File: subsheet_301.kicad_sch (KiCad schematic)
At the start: 12 parts, among them J1601 Like MegaSTE J402, J301 DB-19S ACSI Port, U302 74LS245_PHY, U306 74LS74_PHY, U307 74LS244_PHY

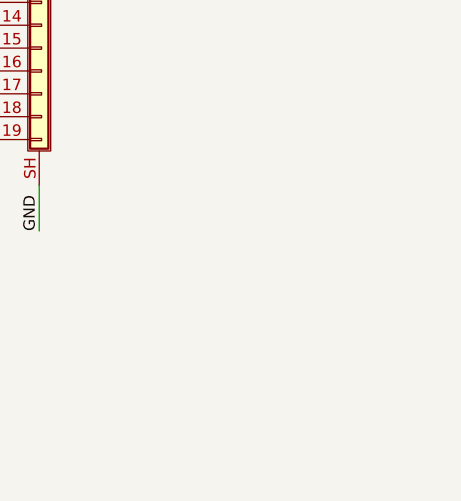
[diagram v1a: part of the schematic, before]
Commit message: add gnd/vcc symbol to start replacing local labels
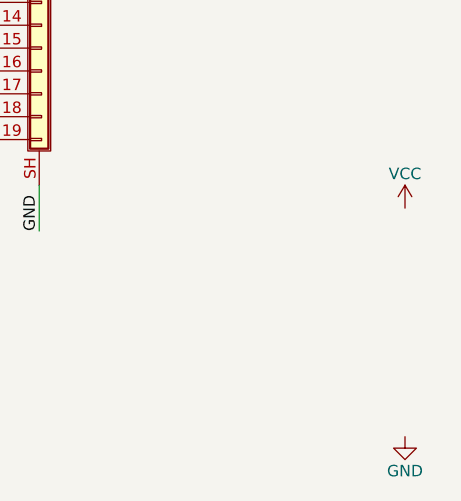
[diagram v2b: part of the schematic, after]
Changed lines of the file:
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@@
     (pin "2")
   )
+  (symbol (lib_id "power:GND") (at 184.15 241.3 0) (unit 1)
+    (in_bom yes) (on_board yes)
+    (property "Reference" "#PWR?" (id 0) (at 184.15 247.65 0)
+      (effects (font (size 1.27 1.27)) hide)
+    )
+    (property "Value" "GND" (id 1) (at 184.15 245.11 0))
+    (property "Footprint" "" (id 2) (at 184.15 241.3 0)
+      (effects (font (size 1.27 1.27)) hide)
+    )
+    (property "Datasheet" "" (id 3) (at 184.15 241.3 0)
+      (effects (font (size 1.27 1.27)) hide)
+    )
+    (pin "1")
+  )
+  (symbol (lib_id "power:VCC") (at 184.15 215.9 0) (unit 1)
+    (in_bom yes) (on_board yes)
+    (property "Reference" "#PWR?" (id 0) (at 184.15 219.71 0)
+      (effects (font (size 1.27 1.27)) hide)
+    )
+    (property "Value" "VCC" (id 1) (at 184.15 212.09 0))
+    (property "Footprint" "" (id 2) (at 184.15 215.9 0)
+      (effects (font (size 1.27 1.27)) hide)
+    )
+    (property "Datasheet" "" (id 3) (at 184.15 215.9 0)
+      (effects (font (size 1.27 1.27)) hide)
+    )
+    (pin "1")
+  )
 )
